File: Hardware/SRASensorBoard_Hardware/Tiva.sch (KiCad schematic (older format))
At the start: 14 parts

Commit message: schematic review meeting
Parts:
- gave numbers to parts that had none: 7
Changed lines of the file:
@@
 $EndDescr
 $Comp
-L MRDT_Shields:TM4C129E_Launchpad U?
+L MRDT_Shields:TM4C129E_Launchpad U3
 U 1 1 614D36F9
 P 2325 2425
-F 0 "U?" H 2350 3725 60  0000 L CNN
+F 0 "U3" H 2350 3725 60  0000 L CNN
 F 1 "TM4C129E_Launchpad" H 1925 3600 60  0000 L CNN
 F 2 "" H 2325 2425 60  0001 C CNN
@@
 $EndComp
 $Comp
-L MRDT_Shields:TM4C129E_Launchpad U?
+L MRDT_Shields:TM4C129E_Launchpad U3
 U 2 1 614D6305
 P 3475 2425
-F 0 "U?" H 3506 3702 60  0000 C CNN
+F 0 "U3" H 3506 3702 60  0000 C CNN
 F 1 "TM4C129E_Launchpad" H 3506 3596 60  0000 C CNN
 F 2 "" H 3475 2425 60  0001 C CNN
@@
 $EndComp
 $Comp
-L MRDT_Shields:TM4C129E_Launchpad U?
+L MRDT_Shields:TM4C129E_Launchpad U3
 U 3 1 614D9ED3
 P 5425 2550
-F 0 "U?" H 5375 3825 60  0000 L CNN
+F 0 "U3" H 5375 3825 60  0000 L CNN
 F 1 "TM4C129E_Launchpad" H 4950 3700 60  0000 L CNN
 F 2 "" H 5425 2550 60  0001 C CNN
@@
 $EndComp
 $Comp
-L MRDT_Shields:TM4C129E_Launchpad U?
+L MRDT_Shields:TM4C129E_Launchpad U3
 U 4 1 614DBFEF
 P 6750 2575
-F 0 "U?" H 6781 3852 60  0000 C CNN
+F 0 "U3" H 6781 3852 60  0000 C CNN
 F 1 "TM4C129E_Launchpad" H 6781 3746 60  0000 C CNN
 F 2 "" H 6750 2575 60  0001 C CNN
@@
 $EndComp
 $Comp
-L MRDT_Shields:TM4C129E_Launchpad U?
+L MRDT_Shields:TM4C129E_Launchpad U3
 U 5 1 614DE0AA
 P 2375 4050
-F 0 "U?" H 2400 5350 60  0000 L CNN
+F 0 "U3" H 2400 5350 60  0000 L CNN
 F 1 "TM4C129E_Launchpad" H 2050 5225 60  0000 L CNN
 F 2 "" H 2375 4050 60  0001 C CNN
@@
 $EndComp
 $Comp
-L MRDT_Shields:TM4C129E_Launchpad U?
+L MRDT_Shields:TM4C129E_Launchpad U3
 U 6 1 614E0749
 P 3625 4050
-F 0 "U?" H 3656 5327 60  0000 C CNN
+F 0 "U3" H 3656 5327 60  0000 C CNN
 F 1 "TM4C129E_Launchpad" H 3656 5221 60  0000 C CNN
 F 2 "" H 3625 4050 60  0001 C CNN
@@
 $EndComp
 $Comp
-L MRDT_Shields:TM4C129E_Launchpad U?
+L MRDT_Shields:TM4C129E_Launchpad U3
 U 7 1 614E25CE
 P 5525 4175
-F 0 "U?" H 5525 5500 60  0000 L CNN
+F 0 "U3" H 5525 5500 60  0000 L CNN
 F 1 "TM4C129E_Launchpad" H 5175 5350 60  0000 L CNN
 F 2 "" H 5525 4175 60  0001 C CNN
@@
 $EndComp
 $Comp
-L MRDT_Shields:TM4C129E_Launchpad U?
+L MRDT_Shields:TM4C129E_Launchpad U3
 U 8 1 614E511C
 P 6775 4175
-F 0 "U?" H 6806 5452 60  0000 C CNN
+F 0 "U3" H 6806 5452 60  0000 C CNN
 F 1 "TM4C129E_Launchpad" H 6806 5346 60  0000 C CNN
 F 2 "" H 6775 4175 60  0001 C CNN
@@
 $EndComp
 $Comp
-L power:GND #PWR?
+L power:GND #PWR0111
 U 1 1 614FF513
 P 7100 3225
-F 0 "#PWR?" H 7100 2975 50  0001 C CNN
-F 1 "GND" V 7105 3097 50  0000 R CNN
+F 0 "#PWR0111" H 7100 2975 50  0001 C CNN
+F 1 "GND" H 7150 3075 50  0000 R CNN
 F 2 "" H 7100 3225 50  0001 C CNN
 F 3 "" H 7100 3225 50  0001 C CNN
 	1    7100 3225
-	0    -1   -1   0
-$EndComp
-$Comp
-L power:GND #PWR?
+	1    0    0    -1
+$EndComp
+$Comp
+L power:GND #PWR0112
 U 1 1 61500297
 P 7100 1625
-F 0 "#PWR?" H 7100 1375 50  0001 C CNN
-F 1 "GND" V 7105 1497 50  0000 R CNN
+F 0 "#PWR0112" H 7100 1375 50  0001 C CNN
+F 1 "GND" H 7150 1450 50  0000 R CNN
 F 2 "" H 7100 1625 50  0001 C CNN
 F 3 "" H 7100 1625 50  0001 C CNN
 	1    7100 1625
-	0    -1   -1   0
-$EndComp
-$Comp
-L power:GND #PWR?
+	1    0    0    -1
+$EndComp
+$Comp
+L power:GND #PWR0113
 U 1 1 61500D9F
 P 3800 1575
-F 0 "#PWR?" H 3800 1325 50  0001 C CNN
-F 1 "GND" V 3805 1447 50  0000 R CNN
+F 0 "#PWR0113" H 3800 1325 50  0001 C CNN
+F 1 "GND" H 3875 1400 50  0000 R CNN
 F 2 "" H 3800 1575 50  0001 C CNN
 F 3 "" H 3800 1575 50  0001 C CNN
 	1    3800 1575
-	0    -1   -1   0
-$EndComp
-$Comp
-L power:GND #PWR?
+	1    0    0    -1
+$EndComp
+$Comp
+L power:GND #PWR0114
 U 1 1 61501306
 P 3950 3200
-F 0 "#PWR?" H 3950 2950 50  0001 C CNN
-F 1 "GND" V 3955 3072 50  0000 R CNN
+F 0 "#PWR0114" H 3950 2950 50  0001 C CNN
+F 1 "GND" H 4025 3050 50  0000 R CNN
 F 2 "" H 3950 3200 50  0001 C CNN
 F 3 "" H 3950 3200 50  0001 C CNN
 	1    3950 3200
-	0    -1   -1   0
+	1    0    0    -1
 $EndComp
 Wire Wire Line
@@
 	3675 1575 3800 1575
 $Comp
-L power:+5V #PWR?
+L power:+5V #PWR0115
 U 1 1 61503CB5
 P 3850 1475
-F 0 "#PWR?" H 3850 1325 50  0001 C CNN
+F 0 "#PWR0115" H 3850 1325 50  0001 C CNN
 F 1 "+5V" H 3865 1648 50  0000 C CNN
 F 2 "" H 3850 1475 50  0001 C CNN
@@
 $EndComp
 $Comp
-L power:+5V #PWR?
+L power:+5V #PWR0116
 U 1 1 615049A2
 P 4000 3100
-F 0 "#PWR?" H 4000 2950 50  0001 C CNN
+F 0 "#PWR0116" H 4000 2950 50  0001 C CNN
 F 1 "+5V" H 4015 3273 50  0000 C CNN
 F 2 "" H 4000 3100 50  0001 C CNN
@@
 	3825 3100 4000 3100
 $Comp
-L power:+3V3 #PWR?
+L power:+3V3 #PWR0117
 U 1 1 61506D3B
 P 1975 1475
-F 0 "#PWR?" H 1975 1325 50  0001 C CNN
+F 0 "#PWR0117" H 1975 1325 50  0001 C CNN
 F 1 "+3V3" H 1990 1648 50  0000 C CNN
 F 2 "" H 1975 1475 50  0001 C CNN
@@
 	1975 1475 2125 1475
 $Comp
-L power:+3V3 #PWR?
+L power:+3V3 #PWR0118
 U 1 1 61507820
 P 2025 3100
-F 0 "#PWR?" H 2025 2950 50  0001 C CNN
+F 0 "#PWR0118" H 2025 2950 50  0001 C CNN
 F 1 "+3V3" H 2040 3273 50  0000 C CNN
 F 2 "" H 2025 3100 50  0001 C CNN
@@
 NoConn ~ 6975 4125
 $Comp
-L Device:LED D?
+L Device:LED D4
 U 1 1 6165658F
 P 1700 3900
-F 0 "D?" H 1800 3950 50  0000 C CNN
+F 0 "D4" H 1800 3950 50  0000 C CNN
 F 1 "LED" H 1925 3950 50  0000 C CNN
 F 2 "" H 1700 3900 50  0001 C CNN
@@
 $EndComp
 $Comp
-L Device:LED D?
+L Device:LED D5
 U 1 1 6165680B
 P 1925 4000
-F 0 "D?" H 2025 3950 50  0000 C CNN
+F 0 "D5" H 2025 3950 50  0000 C CNN
 F 1 "LED" H 2150 3950 50  0000 C CNN
 F 2 "" H 1925 4000 50  0001 C CNN
@@
 	1775 4000 1725 4000
 $Comp
-L Device:R R?
+L Device:R R5
 U 1 1 6165A889
 P 1725 4225
-F 0 "R?" H 1655 4179 50  0000 R CNN
+F 0 "R5" H 1655 4179 50  0000 R CNN
 F 1 "330" V 1725 4300 50  0000 R CNN
 F 2 "" V 1655 4225 50  0001 C CNN
@@
 	1725 4000 1725 4075
 $Comp
-L Device:R R?
+L Device:R R4
 U 1 1 6165C9F3
 P 1500 4225
-F 0 "R?" H 1430 4179 50  0000 R CNN
+F 0 "R4" H 1430 4179 50  0000 R CNN
 F 1 "330" V 1500 4300 50  0000 R CNN
 F 2 "" V 1430 4225 50  0001 C CNN
@@
 $EndComp
 $Comp
-L Device:R R?
+L Device:R R3
 U 1 1 6165CD26
 P 1275 4225
-F 0 "R?" H 1205 4179 50  0000 R CNN
+F 0 "R3" H 1205 4179 50  0000 R CNN
 F 1 "330" V 1275 4300 50  0000 R CNN
 F 2 "" V 1205 4225 50  0001 C CNN
@@
 $EndComp
 $Comp
-L Device:LED D?
+L Device:LED D3
 U 1 1 616555A2
 P 1475 3800
-F 0 "D?" H 1600 3850 50  0000 C CNN
+F 0 "D3" H 1600 3850 50  0000 C CNN
 F 1 "LED" H 1725 3850 50  0000 C CNN
 F 2 "" H 1475 3800 50  0001 C CNN
@@
 	1275 3800 1275 4075
 $Comp
-L power:GND #PWR?
+L power:GND #PWR0119
 U 1 1 61666E76
 P 1500 4500
-F 0 "#PWR?" H 1500 4250 50  0001 C CNN
+F 0 "#PWR0119" H 1500 4250 50  0001 C CNN
 F 1 "GND" H 1505 4327 50  0000 C CNN
 F 2 "" H 1500 4500 50  0001 C CNN
@@
 $EndComp
 $Comp
-L power:GND #PWR?
+L power:GND #PWR0120
 U 1 1 6166AD67
 P 1725 4500
-F 0 "#PWR?" H 1725 4250 50  0001 C CNN
+F 0 "#PWR0120" H 1725 4250 50  0001 C CNN
 F 1 "GND" H 1730 4327 50  0000 C CNN
 F 2 "" H 1725 4500 50  0001 C CNN
@@
 $EndComp
 $Comp
-L power:GND #PWR?
+L power:GND #PWR0121
 U 1 1 6166AEA5
 P 1275 4500
-F 0 "#PWR?" H 1275 4250 50  0001 C CNN
+F 0 "#PWR0121" H 1275 4250 50  0001 C CNN
 F 1 "GND" H 1280 4327 50  0000 C CNN
 F 2 "" H 1275 4500 50  0001 C CNN

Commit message: Labeled LED Colors
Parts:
- D3, D4, D5: value LED -> Blue
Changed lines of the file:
@@
 P 1700 3900
 F 0 "D4" H 1800 3950 50  0000 C CNN
-F 1 "LED" H 1925 3950 50  0000 C CNN
+F 1 "Blue" H 1925 3950 50  0000 C CNN
 F 2 "" H 1700 3900 50  0001 C CNN
 F 3 "~" H 1700 3900 50  0001 C CNN
@@
 P 1925 4000
 F 0 "D5" H 2025 3950 50  0000 C CNN
-F 1 "LED" H 2150 3950 50  0000 C CNN
+F 1 "Blue" H 2150 3950 50  0000 C CNN
 F 2 "" H 1925 4000 50  0001 C CNN
 F 3 "~" H 1925 4000 50  0001 C CNN
@@
 P 1475 3800
 F 0 "D3" H 1600 3850 50  0000 C CNN
-F 1 "LED" H 1725 3850 50  0000 C CNN
+F 1 "Blue" H 1725 3850 50  0000 C CNN
 F 2 "" H 1475 3800 50  0001 C CNN
 F 3 "~" H 1475 3800 50  0001 C CNN

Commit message: Footprint, Layout started
Replaced each 480 ohm resistor with 2 240 ohm resistors b/c we could not find 480 in stock. Footprints for board filled out. Organized components that need to be connected near each other, board placement and wires still need to be done. Board outline created.
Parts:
- D3, D4, D5: footprint (none) -> LED_SMD:LED_0603_1608Metric_Pad1.05x0.95mm_HandSolder
- R3, R4: value 330 -> 43; footprint (none) -> Resistor_SMD:R_0603_1608Metric_Pad1.05x0.95mm_HandSolder
- R5: footprint (none) -> Resistor_SMD:R_0603_1608Metric_Pad1.05x0.95mm_HandSolder
- U3: footprint (none) -> MRDT_Shields:TM4C129E_Launchpad_FULL_Vertical
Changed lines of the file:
@@
 F 0 "U3" H 2350 3725 60  0000 L CNN
 F 1 "TM4C129E_Launchpad" H 1925 3600 60  0000 L CNN
-F 2 "" H 2325 2425 60  0001 C CNN
+F 2 "MRDT_Shields:TM4C129E_Launchpad_FULL_Vertical" H 2325 2425 60  0001 C CNN
 F 3 "" H 2325 2425 60  0001 C CNN
 	1    2325 2425
@@
 F 0 "U3" H 3506 3702 60  0000 C CNN
 F 1 "TM4C129E_Launchpad" H 3506 3596 60  0000 C CNN
-F 2 "" H 3475 2425 60  0001 C CNN
+F 2 "MRDT_Shields:TM4C129E_Launchpad_FULL_Vertical" H 3475 2425 60  0001 C CNN
 F 3 "" H 3475 2425 60  0001 C CNN
 	2    3475 2425
@@
 F 0 "U3" H 5375 3825 60  0000 L CNN
 F 1 "TM4C129E_Launchpad" H 4950 3700 60  0000 L CNN
-F 2 "" H 5425 2550 60  0001 C CNN
+F 2 "MRDT_Shields:TM4C129E_Launchpad_FULL_Vertical" H 5425 2550 60  0001 C CNN
 F 3 "" H 5425 2550 60  0001 C CNN
 	3    5425 2550
@@
 F 0 "U3" H 6781 3852 60  0000 C CNN
 F 1 "TM4C129E_Launchpad" H 6781 3746 60  0000 C CNN
-F 2 "" H 6750 2575 60  0001 C CNN
+F 2 "MRDT_Shields:TM4C129E_Launchpad_FULL_Vertical" H 6750 2575 60  0001 C CNN
 F 3 "" H 6750 2575 60  0001 C CNN
 	4    6750 2575
@@
 F 0 "U3" H 2400 5350 60  0000 L CNN
 F 1 "TM4C129E_Launchpad" H 2050 5225 60  0000 L CNN
-F 2 "" H 2375 4050 60  0001 C CNN
+F 2 "MRDT_Shields:TM4C129E_Launchpad_FULL_Vertical" H 2375 4050 60  0001 C CNN
 F 3 "" H 2375 4050 60  0001 C CNN
 	5    2375 4050
@@
 F 0 "U3" H 3656 5327 60  0000 C CNN
 F 1 "TM4C129E_Launchpad" H 3656 5221 60  0000 C CNN
-F 2 "" H 3625 4050 60  0001 C CNN
+F 2 "MRDT_Shields:TM4C129E_Launchpad_FULL_Vertical" H 3625 4050 60  0001 C CNN
 F 3 "" H 3625 4050 60  0001 C CNN
 	6    3625 4050
@@
 F 0 "U3" H 5525 5500 60  0000 L CNN
 F 1 "TM4C129E_Launchpad" H 5175 5350 60  0000 L CNN
-F 2 "" H 5525 4175 60  0001 C CNN
+F 2 "MRDT_Shields:TM4C129E_Launchpad_FULL_Vertical" H 5525 4175 60  0001 C CNN
 F 3 "" H 5525 4175 60  0001 C CNN
 	7    5525 4175
@@
 F 0 "U3" H 6806 5452 60  0000 C CNN
 F 1 "TM4C129E_Launchpad" H 6806 5346 60  0000 C CNN
-F 2 "" H 6775 4175 60  0001 C CNN
+F 2 "MRDT_Shields:TM4C129E_Launchpad_FULL_Vertical" H 6775 4175 60  0001 C CNN
 F 3 "" H 6775 4175 60  0001 C CNN
 	8    6775 4175
@@
 F 0 "D4" H 1800 3950 50  0000 C CNN
 F 1 "Blue" H 1925 3950 50  0000 C CNN
-F 2 "" H 1700 3900 50  0001 C CNN
+F 2 "LED_SMD:LED_0603_1608Metric_Pad1.05x0.95mm_HandSolder" H 1700 3900 50  0001 C CNN
 F 3 "~" H 1700 3900 50  0001 C CNN
 	1    1700 3900
@@
 F 0 "D5" H 2025 3950 50  0000 C CNN
 F 1 "Blue" H 2150 3950 50  0000 C CNN
-F 2 "" H 1925 4000 50  0001 C CNN
+F 2 "LED_SMD:LED_0603_1608Metric_Pad1.05x0.95mm_HandSolder" H 1925 4000 50  0001 C CNN
 F 3 "~" H 1925 4000 50  0001 C CNN
 	1    1925 4000
@@
 Wire Wire Line
 	1775 4000 1725 4000
-$Comp
-L Device:R R5
-U 1 1 6165A889
-P 1725 4225
-F 0 "R5" H 1655 4179 50  0000 R CNN
-F 1 "330" V 1725 4300 50  0000 R CNN
-F 2 "" V 1655 4225 50  0001 C CNN
-F 3 "~" H 1725 4225 50  0001 C CNN
-	1    1725 4225
-	-1   0    0    1
-$EndComp
 Wire Wire Line
 	1725 4000 1725 4075
@@
 P 1500 4225
 F 0 "R4" H 1430 4179 50  0000 R CNN
-F 1 "330" V 1500 4300 50  0000 R CNN
-F 2 "" V 1430 4225 50  0001 C CNN
+F 1 "43" V 1500 4300 50  0000 R CNN
+F 2 "Resistor_SMD:R_0603_1608Metric_Pad1.05x0.95mm_HandSolder" V 1430 4225 50  0001 C CNN
 F 3 "~" H 1500 4225 50  0001 C CNN
 	1    1500 4225
@@
 P 1275 4225
 F 0 "R3" H 1205 4179 50  0000 R CNN
-F 1 "330" V 1275 4300 50  0000 R CNN
-F 2 "" V 1205 4225 50  0001 C CNN
+F 1 "43" V 1275 4300 50  0000 R CNN
+F 2 "Resistor_SMD:R_0603_1608Metric_Pad1.05x0.95mm_HandSolder" V 1205 4225 50  0001 C CNN
 F 3 "~" H 1275 4225 50  0001 C CNN
 	1    1275 4225
@@
 F 0 "D3" H 1600 3850 50  0000 C CNN
 F 1 "Blue" H 1725 3850 50  0000 C CNN
-F 2 "" H 1475 3800 50  0001 C CNN
+F 2 "LED_SMD:LED_0603_1608Metric_Pad1.05x0.95mm_HandSolder" H 1475 3800 50  0001 C CNN
 F 3 "~" H 1475 3800 50  0001 C CNN
 	1    1475 3800
@@
 Text Notes 1200 4850 0    50   ~ 0
 Software Signals
+$Comp
+L Device:R R5
+U 1 1 6165A889
+P 1725 4225
+F 0 "R5" H 1655 4179 50  0000 R CNN
+F 1 "330" V 1725 4300 50  0000 R CNN
+F 2 "Resistor_SMD:R_0603_1608Metric_Pad1.05x0.95mm_HandSolder" V 1655 4225 50  0001 C CNN
+F 3 "~" H 1725 4225 50  0001 C CNN
+	1    1725 4225
+	-1   0    0    1
+$EndComp
 $EndSCHEMATC

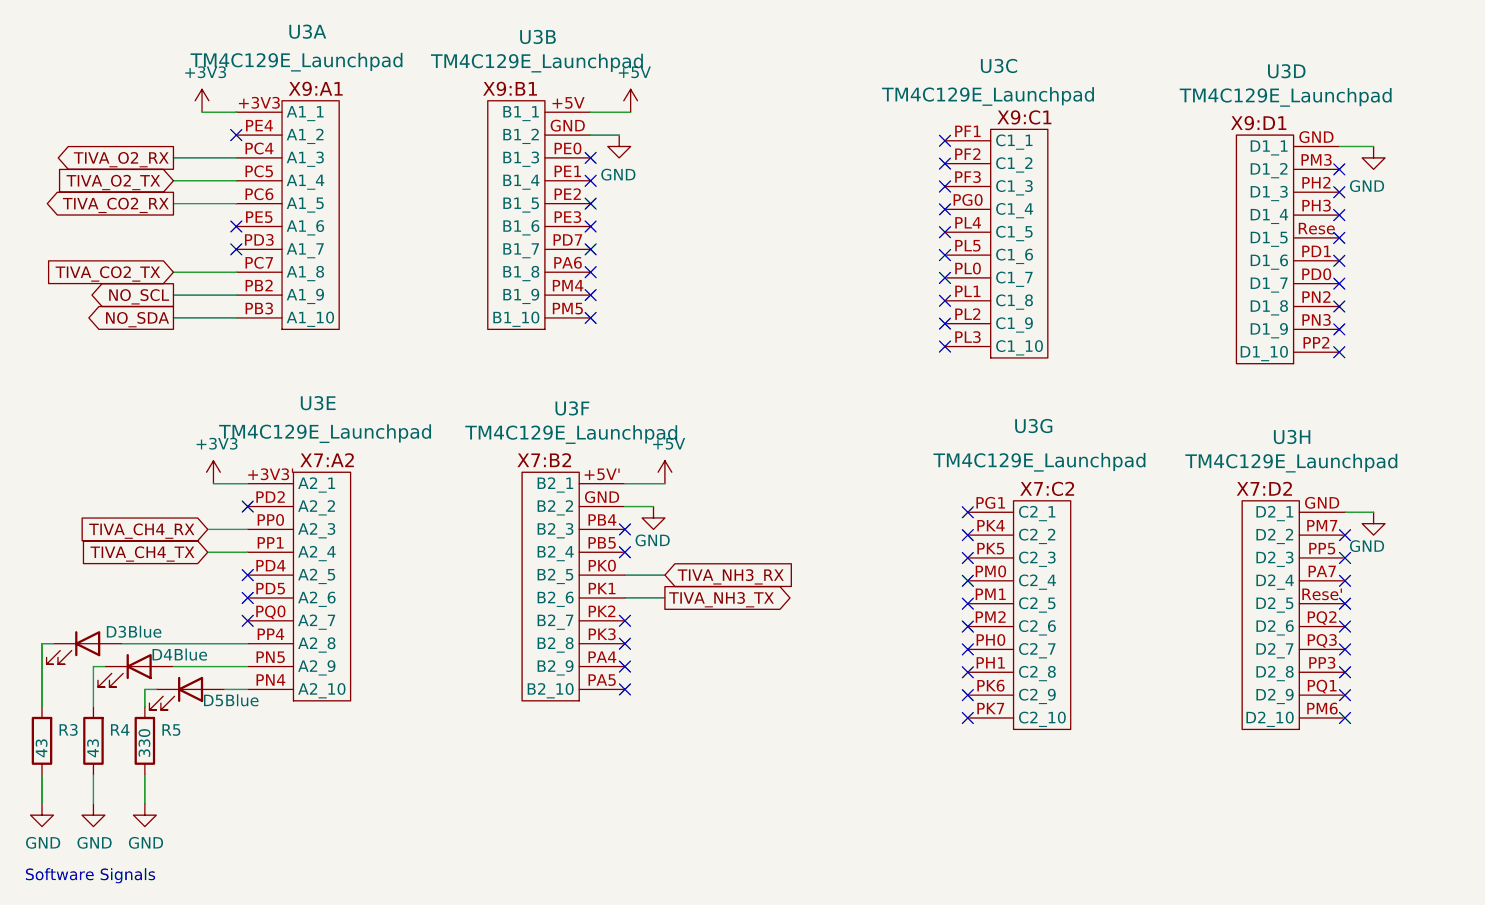
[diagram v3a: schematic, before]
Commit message: Science CDR changes
Changed NO to NO2, removed NH3 data lines for analog output and changed power to 5v, added 3 laser and photodiode pairs (mosfet not determined), added uv and lights connectors, updated tiva pins
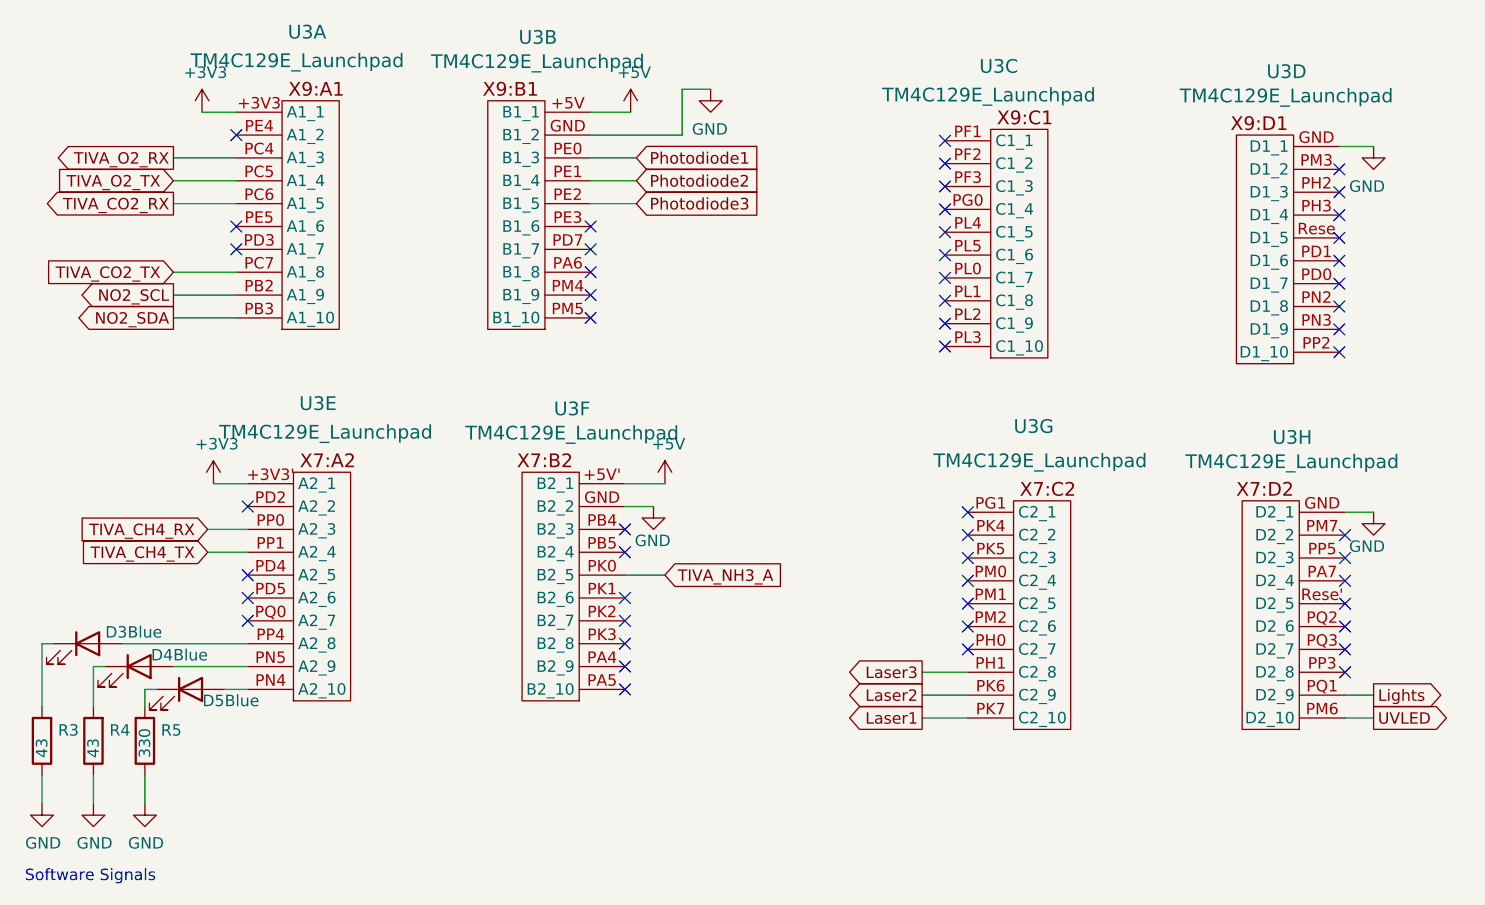
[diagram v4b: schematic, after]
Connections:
- net Photodiode1: now reaches U3.PE0 (B1_3)
- net Photodiode2: now reaches U3.PE1 (B1_4)
- net Photodiode3: now reaches U3.PE2 (B1_5)
- net Laser3: now reaches U3.PH1 (C2_8)
- net Laser2: now reaches U3.PK6 (C2_9)
- net Laser1: now reaches U3.PK7 (C2_10)
- net UVLED: now reaches U3.PM6 (D2_10)
- net Lights: now reaches U3.PQ1 (D2_9)
- net NO_SCL renamed NO2_SCL
- net NO_SDA renamed NO2_SDA
- net TIVA_NH3_RX renamed TIVA_NH3_A
- net TIVA_NH3_TX: no longer names the net of U3.PK1 (B2_6)
- no-connect marks 59 -> 52
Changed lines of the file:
@@
 $Descr A4 11693 8268
 encoding utf-8
-Sheet 2 3
+Sheet 2 4
 Title ""
 Date ""
@@
 L power:GND #PWR0113
 U 1 1 61500D9F
-P 3800 1575
-F 0 "#PWR0113" H 3800 1325 50  0001 C CNN
-F 1 "GND" H 3875 1400 50  0000 R CNN
-F 2 "" H 3800 1575 50  0001 C CNN
-F 3 "" H 3800 1575 50  0001 C CNN
-	1    3800 1575
+P 4200 1375
+F 0 "#PWR0113" H 4200 1125 50  0001 C CNN
+F 1 "GND" H 4275 1200 50  0000 R CNN
+F 2 "" H 4200 1375 50  0001 C CNN
+F 3 "" H 4200 1375 50  0001 C CNN
+	1    4200 1375
 	1    0    0    -1
 $EndComp
@@
 Wire Wire Line
 	3825 3200 3950 3200
-Wire Wire Line
-	3675 1575 3800 1575
 $Comp
 L power:+5V #PWR0115
@@
 	2000 3400 2175 3400
 Text GLabel 1850 2275 0    50   Output ~ 0
-NO_SCL
+NO2_SCL
 Text GLabel 1850 2375 0    50   Output ~ 0
-NO_SDA
+NO2_SDA
 Wire Wire Line
 	2125 2275 1850 2275
@@
 	2125 2375 1850 2375
 Text GLabel 4000 3500 2    50   Input ~ 0
-TIVA_NH3_RX
-Text GLabel 4000 3600 2    50   Output ~ 0
-TIVA_NH3_TX
+TIVA_NH3_A
 Wire Wire Line
 	4000 3500 3825 3500
-Wire Wire Line
-	3825 3600 4000 3600
 NoConn ~ 2125 1575
 NoConn ~ 2125 1975
@@
 NoConn ~ 3675 2075
 NoConn ~ 3675 1975
-NoConn ~ 3675 1875
-NoConn ~ 3675 1775
-NoConn ~ 3675 1675
 NoConn ~ 5225 1600
 NoConn ~ 5225 1700
@@
 NoConn ~ 5325 3525
 NoConn ~ 5325 3625
-NoConn ~ 5325 3725
-NoConn ~ 5325 3825
-NoConn ~ 5325 3925
-NoConn ~ 5325 4025
-NoConn ~ 5325 4125
 NoConn ~ 6975 3325
 NoConn ~ 6975 3425
@@
 NoConn ~ 6975 3825
 NoConn ~ 6975 3925
-NoConn ~ 6975 4025
-NoConn ~ 6975 4125
 $Comp
 L Device:LED D4
@@
 	-1   0    0    1
 $EndComp
+NoConn ~ 3825 3600
+Text GLabel 5125 4125 0    50   Output ~ 0
+Laser1
+Text GLabel 5125 4025 0    50   Output ~ 0
+Laser2
+Text GLabel 5125 3925 0    50   Output ~ 0
+Laser3
+Text GLabel 7100 4025 2    50   Output ~ 0
+Lights
+Text GLabel 7100 4125 2    50   Output ~ 0
+UVLED
+NoConn ~ 5325 3725
+NoConn ~ 5325 3825
+Wire Wire Line
+	5125 4125 5325 4125
+Wire Wire Line
+	5325 4025 5125 4025
+Wire Wire Line
+	5125 3925 5325 3925
+Wire Wire Line
+	6975 4125 7100 4125
+Wire Wire Line
+	7100 4025 6975 4025
+Text GLabel 3875 1675 2    51   Input ~ 0
+Photodiode1
+Text GLabel 3875 1775 2    51   Input ~ 0
+Photodiode2
+Text GLabel 3875 1875 2    51   Input ~ 0
+Photodiode3
+Wire Wire Line
+	3675 1575 4075 1575
+Wire Wire Line
+	4075 1575 4075 1375
+Wire Wire Line
+	4075 1375 4200 1375
+Wire Wire Line
+	3675 1675 3875 1675
+Wire Wire Line
+	3675 1775 3875 1775
+Wire Wire Line
+	3675 1875 3875 1875
 $EndSCHEMATC
